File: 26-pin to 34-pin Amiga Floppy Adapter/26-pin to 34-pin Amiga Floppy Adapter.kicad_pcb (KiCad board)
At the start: 2 copper layers, 71.1 x 39.4 mm, 7 parts, among them CN1 Conn_02x13_Odd_Even, CN2 Conn_02x17_Odd_Even, CN3 Conn_01x04

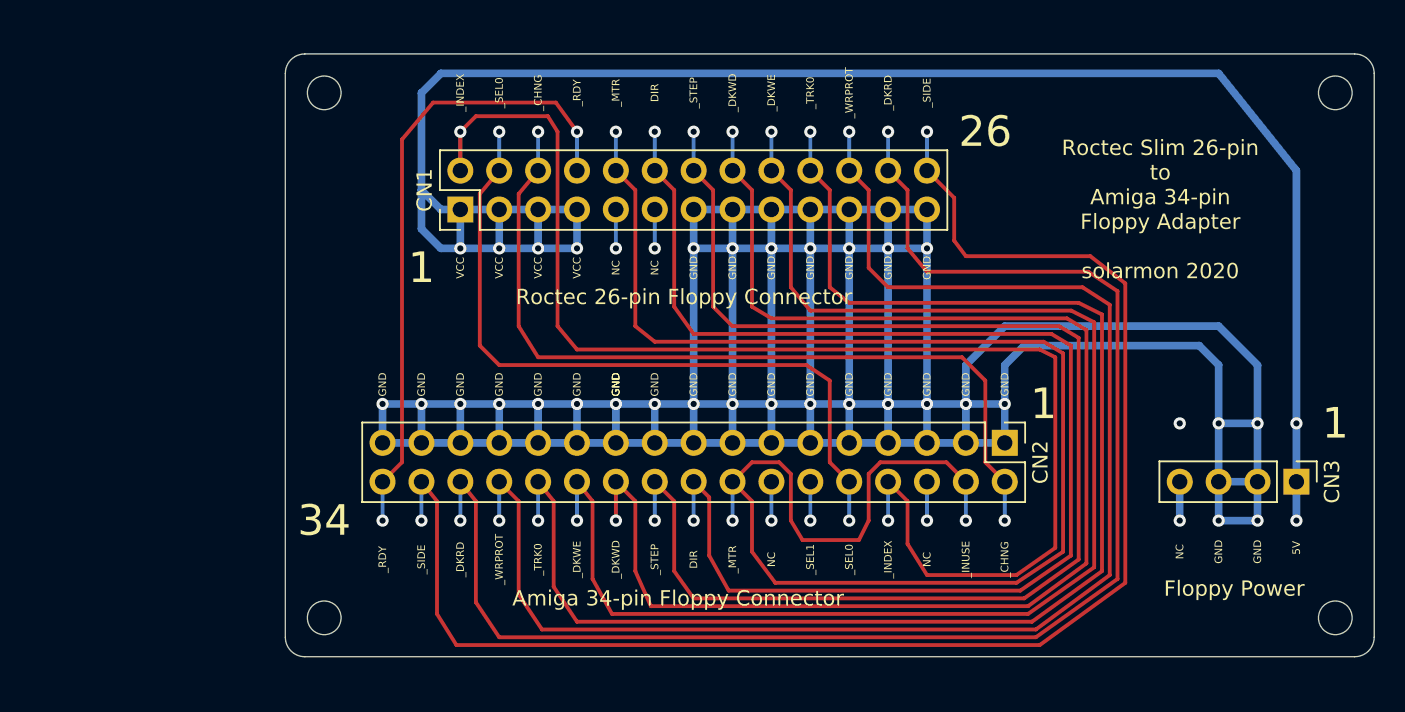
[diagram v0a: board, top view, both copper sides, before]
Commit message: Some improvements
Made bottom side a filled zone for GND and moved floppy power connector to other side for shorter VCC tracks.
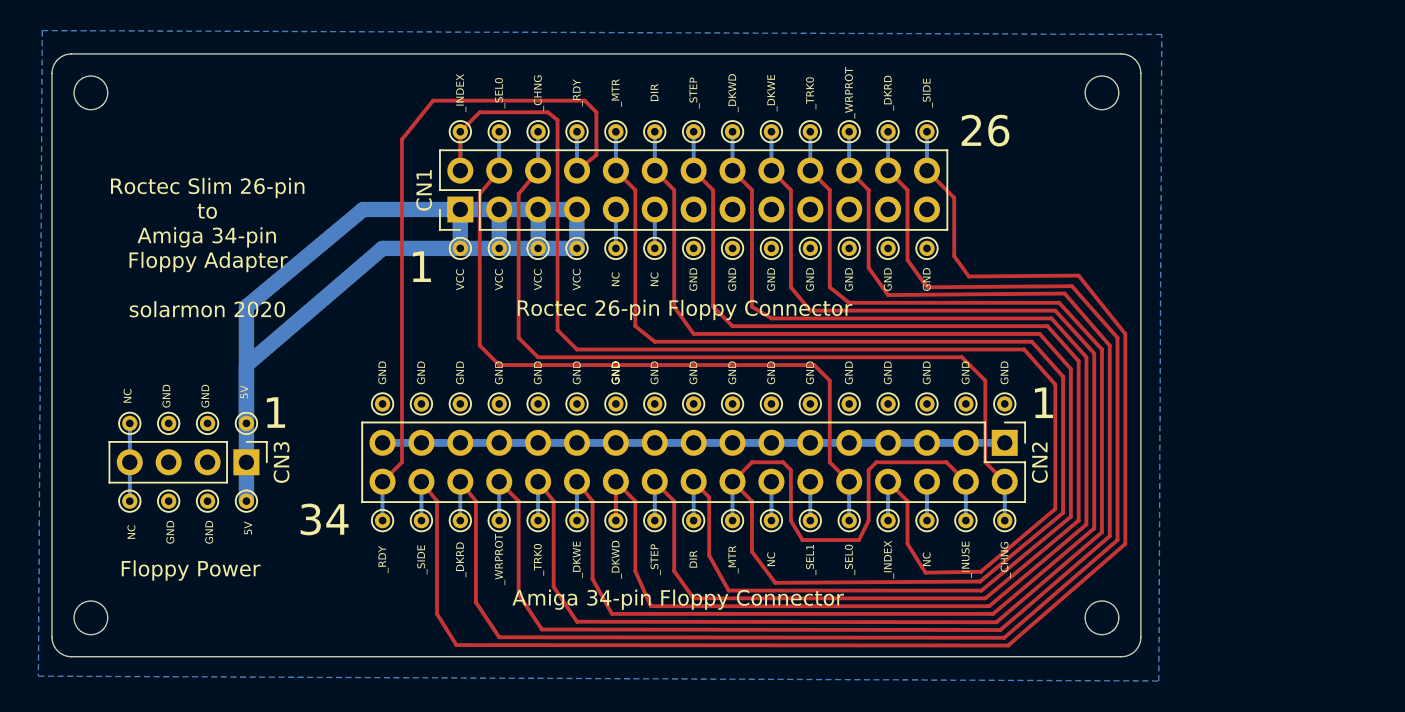
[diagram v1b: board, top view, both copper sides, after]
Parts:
- added ?: TestPoint_THTPad_D1.0mm_Drill0.5mm, TestPoint:TestPoint_THTPad_D1.0mm_Drill0.5mm, F.Cu at (132.1, 97.8)
- added ?: TestPoint_THTPad_D1.0mm_Drill0.5mm, TestPoint:TestPoint_THTPad_D1.0mm_Drill0.5mm, F.Cu at (116.8, 108.0)
- added ?: TestPoint_THTPad_D1.0mm_Drill0.5mm, TestPoint:TestPoint_THTPad_D1.0mm_Drill0.5mm, F.Cu at (119.4, 108.0)
- added ?: TestPoint_THTPad_D1.0mm_Drill0.5mm, TestPoint:TestPoint_THTPad_D1.0mm_Drill0.5mm, F.Cu at (121.9, 108.0)
- added ?: TestPoint_THTPad_D1.0mm_Drill0.5mm, TestPoint:TestPoint_THTPad_D1.0mm_Drill0.5mm, F.Cu at (124.5, 108.0)
- added ?: TestPoint_THTPad_D1.0mm_Drill0.5mm, TestPoint:TestPoint_THTPad_D1.0mm_Drill0.5mm, F.Cu at (127.0, 108.0)
- added ?: TestPoint_THTPad_D1.0mm_Drill0.5mm, TestPoint:TestPoint_THTPad_D1.0mm_Drill0.5mm, F.Cu at (129.5, 108.0)
- added ?: TestPoint_THTPad_D1.0mm_Drill0.5mm, TestPoint:TestPoint_THTPad_D1.0mm_Drill0.5mm, F.Cu at (132.1, 108.0)
- added ?: TestPoint_THTPad_D1.0mm_Drill0.5mm, TestPoint:TestPoint_THTPad_D1.0mm_Drill0.5mm, F.Cu at (134.6, 108.0)
- added ?: TestPoint_THTPad_D1.0mm_Drill0.5mm, TestPoint:TestPoint_THTPad_D1.0mm_Drill0.5mm, F.Cu at (137.2, 108.0)
- added ?: TestPoint_THTPad_D1.0mm_Drill0.5mm, TestPoint:TestPoint_THTPad_D1.0mm_Drill0.5mm, F.Cu at (139.7, 108.0)
- added ?: TestPoint_THTPad_D1.0mm_Drill0.5mm, TestPoint:TestPoint_THTPad_D1.0mm_Drill0.5mm, F.Cu at (134.6, 97.8)
- added ?: TestPoint_THTPad_D1.0mm_Drill0.5mm, TestPoint:TestPoint_THTPad_D1.0mm_Drill0.5mm, F.Cu at (142.2, 108.0)
- added ?: TestPoint_THTPad_D1.0mm_Drill0.5mm, TestPoint:TestPoint_THTPad_D1.0mm_Drill0.5mm, F.Cu at (144.8, 108.0)
- added ?: TestPoint_THTPad_D1.0mm_Drill0.5mm, TestPoint:TestPoint_THTPad_D1.0mm_Drill0.5mm, F.Cu at (147.3, 90.2)
- added ?: TestPoint_THTPad_D1.0mm_Drill0.5mm, TestPoint:TestPoint_THTPad_D1.0mm_Drill0.5mm, F.Cu at (144.8, 90.2)
- added ?: TestPoint_THTPad_D1.0mm_Drill0.5mm, TestPoint:TestPoint_THTPad_D1.0mm_Drill0.5mm, F.Cu at (142.2, 90.2)
- added ?: TestPoint_THTPad_D1.0mm_Drill0.5mm, TestPoint:TestPoint_THTPad_D1.0mm_Drill0.5mm, F.Cu at (139.7, 90.2)
- added ?: TestPoint_THTPad_D1.0mm_Drill0.5mm, TestPoint:TestPoint_THTPad_D1.0mm_Drill0.5mm, F.Cu at (137.2, 90.2)
- added ?: TestPoint_THTPad_D1.0mm_Drill0.5mm, TestPoint:TestPoint_THTPad_D1.0mm_Drill0.5mm, F.Cu at (134.6, 90.2)
- added ?: TestPoint_THTPad_D1.0mm_Drill0.5mm, TestPoint:TestPoint_THTPad_D1.0mm_Drill0.5mm, F.Cu at (132.1, 90.2)
- added ?: TestPoint_THTPad_D1.0mm_Drill0.5mm, TestPoint:TestPoint_THTPad_D1.0mm_Drill0.5mm, F.Cu at (129.5, 90.2)
- added ?: TestPoint_THTPad_D1.0mm_Drill0.5mm, TestPoint:TestPoint_THTPad_D1.0mm_Drill0.5mm, F.Cu at (137.2, 97.8)
- added ?: TestPoint_THTPad_D1.0mm_Drill0.5mm, TestPoint:TestPoint_THTPad_D1.0mm_Drill0.5mm, F.Cu at (127.0, 90.2)
- added ?: TestPoint_THTPad_D1.0mm_Drill0.5mm, TestPoint:TestPoint_THTPad_D1.0mm_Drill0.5mm, F.Cu at (124.5, 90.2)
- added ?: TestPoint_THTPad_D1.0mm_Drill0.5mm, TestPoint:TestPoint_THTPad_D1.0mm_Drill0.5mm, F.Cu at (121.9, 90.2)
- added ?: TestPoint_THTPad_D1.0mm_Drill0.5mm, TestPoint:TestPoint_THTPad_D1.0mm_Drill0.5mm, F.Cu at (119.4, 90.2)
- added ?: TestPoint_THTPad_D1.0mm_Drill0.5mm, TestPoint:TestPoint_THTPad_D1.0mm_Drill0.5mm, F.Cu at (116.8, 90.2)
- added ?: TestPoint_THTPad_D1.0mm_Drill0.5mm, TestPoint:TestPoint_THTPad_D1.0mm_Drill0.5mm, F.Cu at (129.5, 97.8)
- added ?: TestPoint_THTPad_D1.0mm_Drill0.5mm, TestPoint:TestPoint_THTPad_D1.0mm_Drill0.5mm, F.Cu at (127.0, 97.8)
- added ?: TestPoint_THTPad_D1.0mm_Drill0.5mm, TestPoint:TestPoint_THTPad_D1.0mm_Drill0.5mm, F.Cu at (124.5, 97.8)
- added ?: TestPoint_THTPad_D1.0mm_Drill0.5mm, TestPoint:TestPoint_THTPad_D1.0mm_Drill0.5mm, F.Cu at (121.9, 97.8)
- added ?: TestPoint_THTPad_D1.0mm_Drill0.5mm, TestPoint:TestPoint_THTPad_D1.0mm_Drill0.5mm, F.Cu at (119.4, 97.8)
- added ?: TestPoint_THTPad_D1.0mm_Drill0.5mm, TestPoint:TestPoint_THTPad_D1.0mm_Drill0.5mm, F.Cu at (139.7, 97.8)
- added ?: TestPoint_THTPad_D1.0mm_Drill0.5mm, TestPoint:TestPoint_THTPad_D1.0mm_Drill0.5mm, F.Cu at (116.8, 97.8)
- added ?: TestPoint_THTPad_D1.0mm_Drill0.5mm, TestPoint:TestPoint_THTPad_D1.0mm_Drill0.5mm, F.Cu at (102.9, 114.3)
- added ?: TestPoint_THTPad_D1.0mm_Drill0.5mm, TestPoint:TestPoint_THTPad_D1.0mm_Drill0.5mm, F.Cu at (100.3, 114.3)
- added ?: TestPoint_THTPad_D1.0mm_Drill0.5mm, TestPoint:TestPoint_THTPad_D1.0mm_Drill0.5mm, F.Cu at (97.8, 114.3)
- added ?: TestPoint_THTPad_D1.0mm_Drill0.5mm, TestPoint:TestPoint_THTPad_D1.0mm_Drill0.5mm, F.Cu at (95.2, 114.3)
- added ?: TestPoint_THTPad_D1.0mm_Drill0.5mm, TestPoint:TestPoint_THTPad_D1.0mm_Drill0.5mm, F.Cu at (95.2, 109.2)
- added ?: TestPoint_THTPad_D1.0mm_Drill0.5mm, TestPoint:TestPoint_THTPad_D1.0mm_Drill0.5mm, F.Cu at (102.9, 109.2)
- added ?: TestPoint_THTPad_D1.0mm_Drill0.5mm, TestPoint:TestPoint_THTPad_D1.0mm_Drill0.5mm, F.Cu at (100.3, 109.2)
- added ?: TestPoint_THTPad_D1.0mm_Drill0.5mm, TestPoint:TestPoint_THTPad_D1.0mm_Drill0.5mm, F.Cu at (97.8, 109.2)
- added ?: TestPoint_THTPad_D1.0mm_Drill0.5mm, TestPoint:TestPoint_THTPad_D1.0mm_Drill0.5mm, F.Cu at (147.3, 108.0)
- added ?: TestPoint_THTPad_D1.0mm_Drill0.5mm, TestPoint:TestPoint_THTPad_D1.0mm_Drill0.5mm, F.Cu at (142.2, 97.8)
- added ?: TestPoint_THTPad_D1.0mm_Drill0.5mm, TestPoint:TestPoint_THTPad_D1.0mm_Drill0.5mm, F.Cu at (149.9, 108.0)
- added ?: TestPoint_THTPad_D1.0mm_Drill0.5mm, TestPoint:TestPoint_THTPad_D1.0mm_Drill0.5mm, F.Cu at (152.4, 108.0)
- added ?: TestPoint_THTPad_D1.0mm_Drill0.5mm, TestPoint:TestPoint_THTPad_D1.0mm_Drill0.5mm, F.Cu at (111.8, 115.6)
- added ?: TestPoint_THTPad_D1.0mm_Drill0.5mm, TestPoint:TestPoint_THTPad_D1.0mm_Drill0.5mm, F.Cu at (114.3, 115.6)
- added ?: TestPoint_THTPad_D1.0mm_Drill0.5mm, TestPoint:TestPoint_THTPad_D1.0mm_Drill0.5mm, F.Cu at (116.8, 115.6)
- added ?: TestPoint_THTPad_D1.0mm_Drill0.5mm, TestPoint:TestPoint_THTPad_D1.0mm_Drill0.5mm, F.Cu at (119.4, 115.6)
- added ?: TestPoint_THTPad_D1.0mm_Drill0.5mm, TestPoint:TestPoint_THTPad_D1.0mm_Drill0.5mm, F.Cu at (121.9, 115.6)
- added ?: TestPoint_THTPad_D1.0mm_Drill0.5mm, TestPoint:TestPoint_THTPad_D1.0mm_Drill0.5mm, F.Cu at (124.5, 115.6)
- added ?: TestPoint_THTPad_D1.0mm_Drill0.5mm, TestPoint:TestPoint_THTPad_D1.0mm_Drill0.5mm, F.Cu at (127.0, 115.6)
- added ?: TestPoint_THTPad_D1.0mm_Drill0.5mm, TestPoint:TestPoint_THTPad_D1.0mm_Drill0.5mm, F.Cu at (129.5, 115.6)
- added ?: TestPoint_THTPad_D1.0mm_Drill0.5mm, TestPoint:TestPoint_THTPad_D1.0mm_Drill0.5mm, F.Cu at (144.8, 97.8)
- added ?: TestPoint_THTPad_D1.0mm_Drill0.5mm, TestPoint:TestPoint_THTPad_D1.0mm_Drill0.5mm, F.Cu at (132.1, 115.6)
- added ?: TestPoint_THTPad_D1.0mm_Drill0.5mm, TestPoint:TestPoint_THTPad_D1.0mm_Drill0.5mm, F.Cu at (134.6, 115.6)
- added ?: TestPoint_THTPad_D1.0mm_Drill0.5mm, TestPoint:TestPoint_THTPad_D1.0mm_Drill0.5mm, F.Cu at (137.2, 115.6)
- added ?: TestPoint_THTPad_D1.0mm_Drill0.5mm, TestPoint:TestPoint_THTPad_D1.0mm_Drill0.5mm, F.Cu at (139.7, 115.6)
- added ?: TestPoint_THTPad_D1.0mm_Drill0.5mm, TestPoint:TestPoint_THTPad_D1.0mm_Drill0.5mm, F.Cu at (142.2, 115.6)
- added ?: TestPoint_THTPad_D1.0mm_Drill0.5mm, TestPoint:TestPoint_THTPad_D1.0mm_Drill0.5mm, F.Cu at (144.8, 115.6)
- added ?: TestPoint_THTPad_D1.0mm_Drill0.5mm, TestPoint:TestPoint_THTPad_D1.0mm_Drill0.5mm, F.Cu at (147.3, 115.6)
- added ?: TestPoint_THTPad_D1.0mm_Drill0.5mm, TestPoint:TestPoint_THTPad_D1.0mm_Drill0.5mm, F.Cu at (149.9, 115.6)
- added ?: TestPoint_THTPad_D1.0mm_Drill0.5mm, TestPoint:TestPoint_THTPad_D1.0mm_Drill0.5mm, F.Cu at (152.4, 115.6)
- added ?: TestPoint_THTPad_D1.0mm_Drill0.5mm, TestPoint:TestPoint_THTPad_D1.0mm_Drill0.5mm, F.Cu at (147.3, 97.8)
- added ?: TestPoint_THTPad_D1.0mm_Drill0.5mm, TestPoint:TestPoint_THTPad_D1.0mm_Drill0.5mm, F.Cu at (111.8, 108.0)
- added ?: TestPoint_THTPad_D1.0mm_Drill0.5mm, TestPoint:TestPoint_THTPad_D1.0mm_Drill0.5mm, F.Cu at (114.3, 108.0)
- moved CN3 68.6 mm to (102.9, 111.8)
- moved ? 15.2 mm to (92.7, 87.6)
- moved ? 15.2 mm to (92.7, 121.9)
- moved ? 15.2 mm to (158.8, 121.9)
- moved ? 15.2 mm to (158.8, 87.6)
- renumbered REF** to ?
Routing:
- net GND: track 313.0 -> 40.6 mm, vias 28 -> 0
- net VCC: track 124.0 -> 75.0 mm, vias 6 -> 0
- net /_RDY: track 41.5 -> 46.6 mm, vias 2 -> 0
- net /_TRK0: track 93.6 -> 91.1 mm, vias 2 -> 0
- net Net-(CN3-Pad4): track 2.54 -> 5.08 mm, vias 1 -> 0
- net /_WRPROT: track 95.1 -> 92.6 mm, vias 2 -> 0
- net /_DKWE: track 91.7 -> 89.3 mm, vias 2 -> 0
- net /_DKWD: track 92.8 -> 90.4 mm, vias 2 -> 0
- net /_DKRD: track 96.9 -> 94.5 mm, vias 2 -> 0
- net /_SIDE: track 98.6 -> 96.4 mm, vias 2 -> 0
- net /DIR: track 86.2 -> 83.9 mm, vias 2 -> 0
- net /_STEP: track 88.1 -> 85.9 mm, vias 2 -> 0
- net /_INDEX: track 89.4 -> 87.4 mm, vias 2 -> 0
- net /_INUSE: track 111.3 -> 109.4 mm, vias 3 -> 0
- net /_CHNG: track 55.1 -> 55.2 mm, vias 2 -> 0
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- added copper zone on B.Cu, net GND
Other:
- outline, holes or cut-outs redrawn
- net class VCC added: clearance 0.2, trace_width 1, via_dia 0.8, via_drill 0.4

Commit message: More improvements
* Improved GND net points
* Test points in appropropriate nets
* Added additional VCC trace
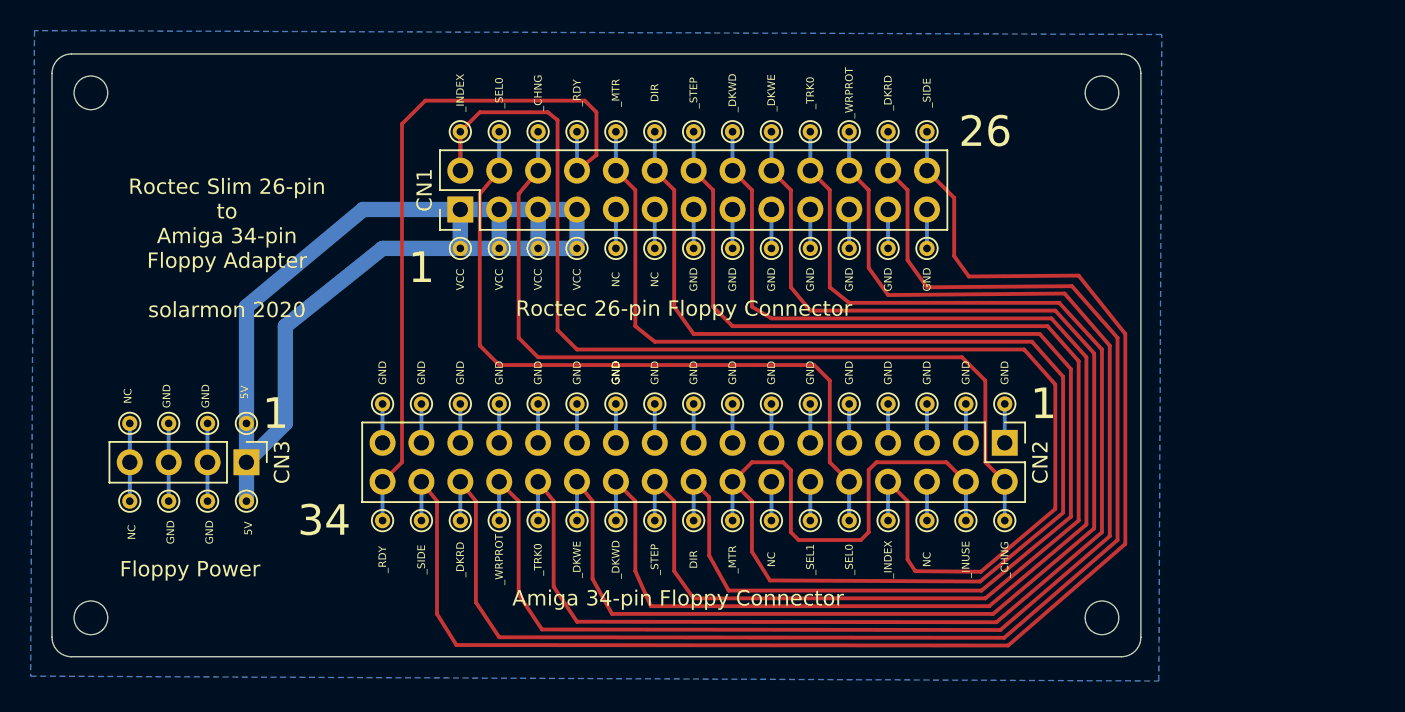
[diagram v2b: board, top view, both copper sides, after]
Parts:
- turned ? to 90 degrees
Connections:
- ? pad : (no net) -> /_RDY
- ? pad : (no net) -> /_SIDE
- ? pad : (no net) -> /_DKRD
- ? pad : (no net) -> /_WRPROT
- ? pad : (no net) -> /_TRK0
- ? pad : (no net) -> /_DKWE
- ? pad : (no net) -> /_STEP
- ? pad : (no net) -> /DIR
- ? pad : (no net) -> /_INUSE
- ? pad : (no net) -> Net-(CN2-Pad14)
- ? pad : (no net) -> /_SEL1
- ? pad : (no net) -> /_SEL0
- ? pad : (no net) -> /_INDEX
- ? pad : (no net) -> Net-(CN2-Pad6)
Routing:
- net GND: track 40.6 -> 71.1 mm
- net VCC: track 75.0 -> 77.5 mm
- net /_DKWD: track 90.4 -> 87.9 mm
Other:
- net class GND added: clearance 0.2, trace_width 0.5, via_dia 0.8, via_drill 0.4

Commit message: Added VCC zone
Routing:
- added copper zone on B.Cu, net VCC
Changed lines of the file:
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@@
   (page A4)
   (layers
-    (0 F.Cu signal hide)
+    (0 F.Cu signal)
     (31 B.Cu signal)
     (32 B.Adhes user)
@@
       )
     )
+  )
+  (zone (net 14) (net_name VCC) (layer B.Cu) (hatch edge 0.508)
+    (connect_pads (clearance 0.508))
+    (min_thickness 0.254)
+    (fill yes (arc_segments 32) (thermal_gap 0.508) (thermal_bridge_width 0.508))
+    (polygon
+      (pts
+        (xy 124.46 97.79) (xy 124.46 95.25) (xy 110.49 95.25) (xy 102.87 101.6) (xy 102.87 111.76)
+        (xy 105.41 109.22) (xy 105.41 102.87) (xy 111.76 97.79)
+      )
+    )
